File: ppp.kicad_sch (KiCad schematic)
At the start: 0 parts

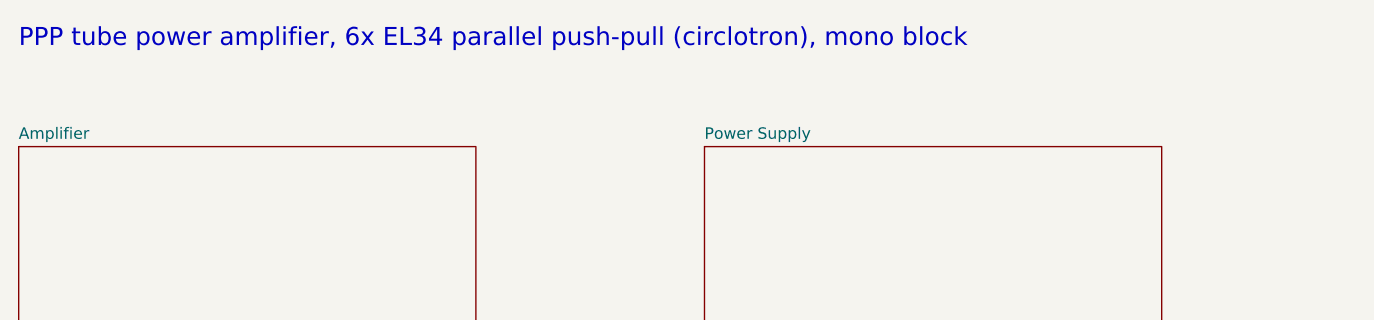
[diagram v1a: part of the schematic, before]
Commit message: KT88 variant: 4x KT88 instead of 6x EL34
- New ppp:KT88 symbol (beam tetrode, pin 1 n.c., no G3 pin)
- V3-V6 -> KT88, G3-cathode links removed
- Third output column removed (V7, V8, C13, C14, R23, R24, R29, R30,
  R35, R36, R41, R42, R47, R48, P5, P6)
- Grid leaks R19-R22 220k -> 150k (KT88 fixed-bias Rg1 max)
- Titles/notes updated, PDF regenerated
- KT88.md: feasibility analysis and open points

Co-Authored-By: Claude Opus 5.5 <noreply@anthropic.com>
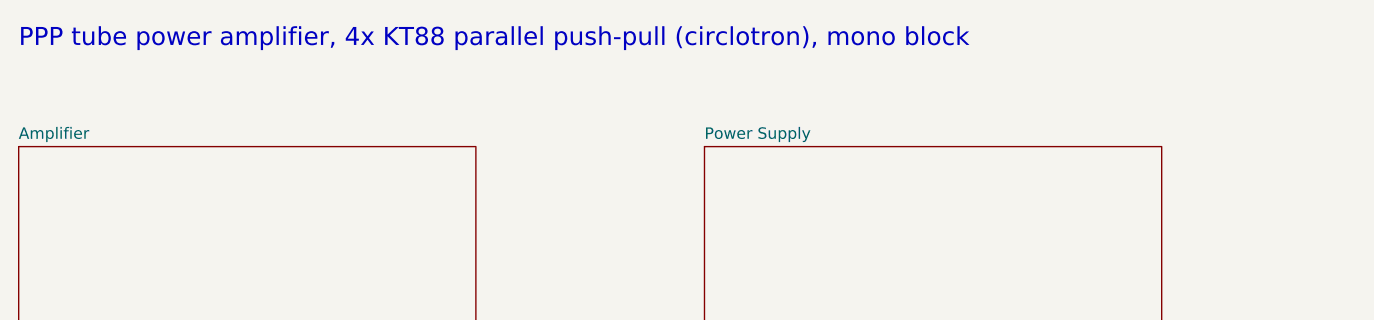
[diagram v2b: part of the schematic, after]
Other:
- note added: "PPP tube power amplifier, 4x KT88 parallel push-pull (circlotron), mono block"
- note removed: "PPP tube power amplifier, 6x EL34 parallel push-pull (circlotron), mono block"
- title: PPP power amplifier 6x EL34 (mono) -> PPP power amplifier 4x KT88 (mono)
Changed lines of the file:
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@@
 	(paper "A4")
 	(title_block
-		(title "PPP power amplifier 6x EL34 (mono)")
+		(title "PPP power amplifier 4x KT88 (mono)")
 		(date "2026-10-20")
 		(rev "1")
@@
 		)
 	)
-	(text "PPP tube power amplifier, 6x EL34 parallel push-pull (circlotron), mono block"
+	(text "PPP tube power amplifier, 4x KT88 parallel push-pull (circlotron), mono block"
 		(exclude_from_sim no)
 		(at 50.8 40 0)

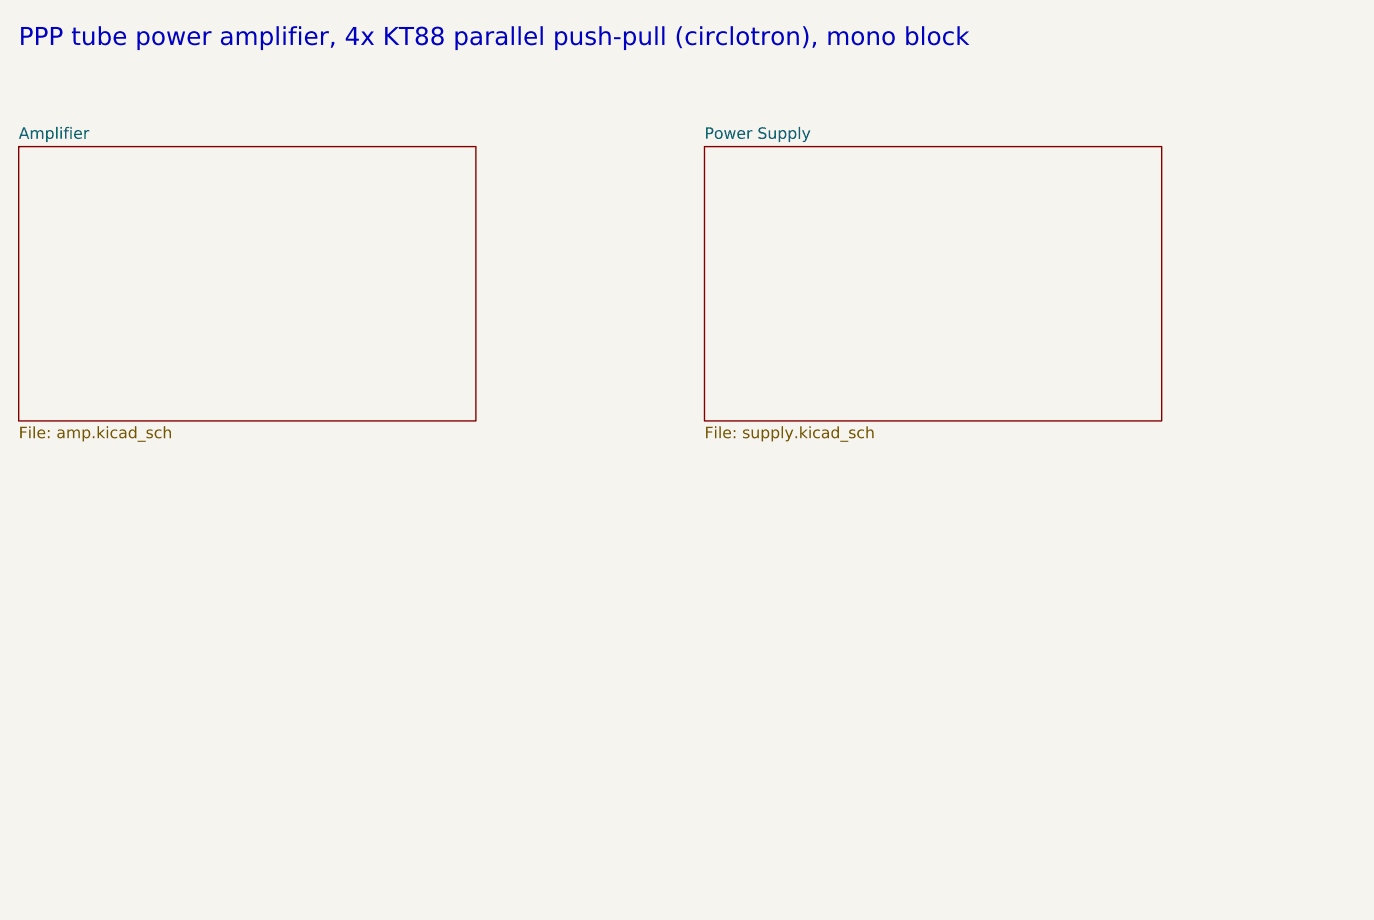
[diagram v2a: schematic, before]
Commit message: SMPS variant: draft schematic replacing the mains supply
Replace supply.kicad_sch with two sheets:
- smps_pri: mains input/EMI filter, NTC + relay bypass, UC3854B PFC
  (390 V bus), fixed-frequency LLC half-bridge (UCC25600 + UCC27714),
  current transformer, startup and aux supply, bus-OK logic.
- smps_sec: T201, both bank supplies (SiC bridge, CM choke, cap
  multiplier, 52 s B+ delay), heater buck synced from W3.

Net labels to the amp sheet are unchanged; D5/D6 become UF4007 for the
100 kHz bias windings. Adds T_SMPS_PPP and UC3854B symbols. Values are
start values; see SMPS.md for open points.

Co-Authored-By: Claude Opus 5.5 <noreply@anthropic.com>
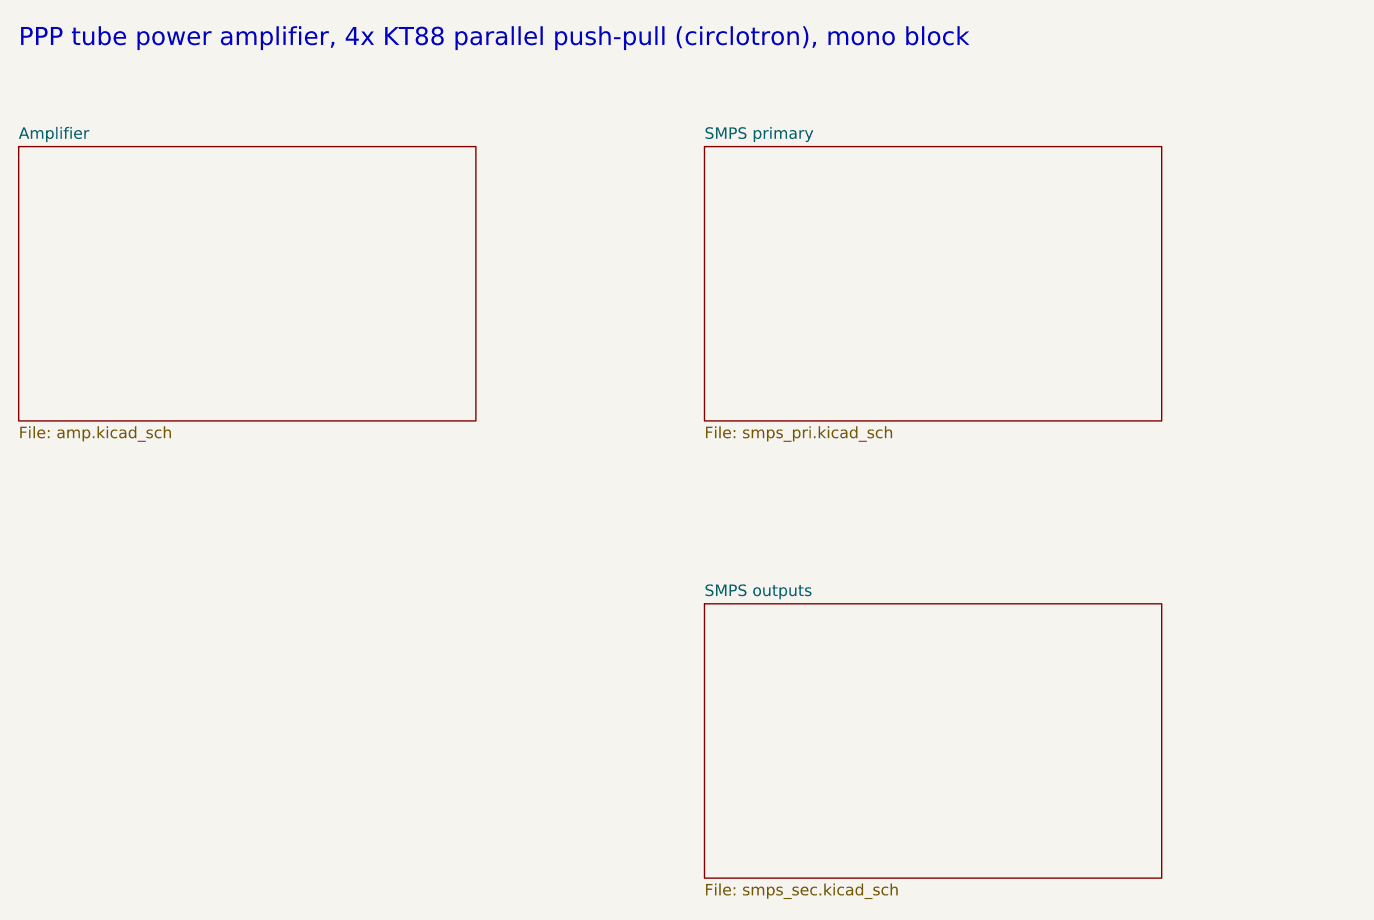
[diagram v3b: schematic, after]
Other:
- removed sheet Power Supply
- added sheet SMPS outputs (smps_sec.kicad_sch)
- added sheet SMPS primary (smps_pri.kicad_sch)
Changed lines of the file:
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@@
 			(color 0 0 0 0)
 		)
-		(property "Sheetname" "Power Supply"
+		(property "Sheetname" "SMPS primary"
 			(at 127 50.0884 0)
 			(effects
@@
 			)
 		)
-		(property "Sheetfile" "supply.kicad_sch"
+		(property "Sheetfile" "smps_pri.kicad_sch"
 			(at 127 81.8646 0)
 			(effects
@@
 				)
 			)
+		)
+	)
+	(sheet
+		(at 127 101.6)
+		(size 50.8 30.48)
+		(exclude_from_sim no)
+		(in_bom yes)
+		(on_board yes)
+		(dnp no)
+		(fields_autoplaced yes)
+		(stroke
+			(width 0.1524)
+			(type solid)
+		)
+		(fill
+			(color 0 0 0 0)
+		)
+		(property "Sheetname" "SMPS outputs"
+			(at 127 100.8884 0)
+			(effects
+				(font
+					(size 1.27 1.27)
+				)
+				(justify left bottom)
+			)
+		)
+		(property "Sheetfile" "smps_sec.kicad_sch"
+			(at 127 132.6646 0)
+			(effects
+				(font
+					(size 1.27 1.27)
+				)
+				(justify left top)
+			)
+		)
+		(instances
+			(project "ppp"
+				(path "/b1cb1816-7d85-457c-9f32-2a1422d00e17"
+					(page "4")
+				)
+			)
